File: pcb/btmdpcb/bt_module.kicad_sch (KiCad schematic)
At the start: 21 parts, among them J2 ANT, T1 ED8_4, T2 ED8_4

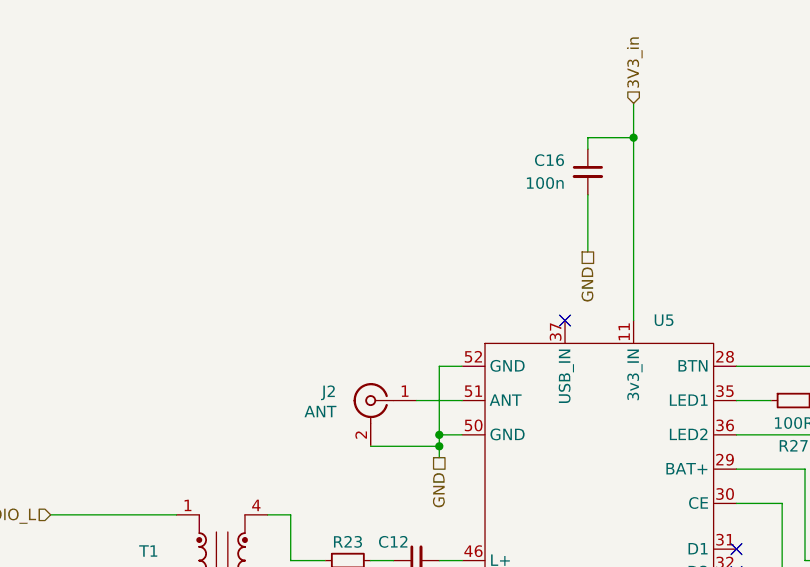
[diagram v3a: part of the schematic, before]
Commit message: Correct footprints, fix issues on update PCB from schematic
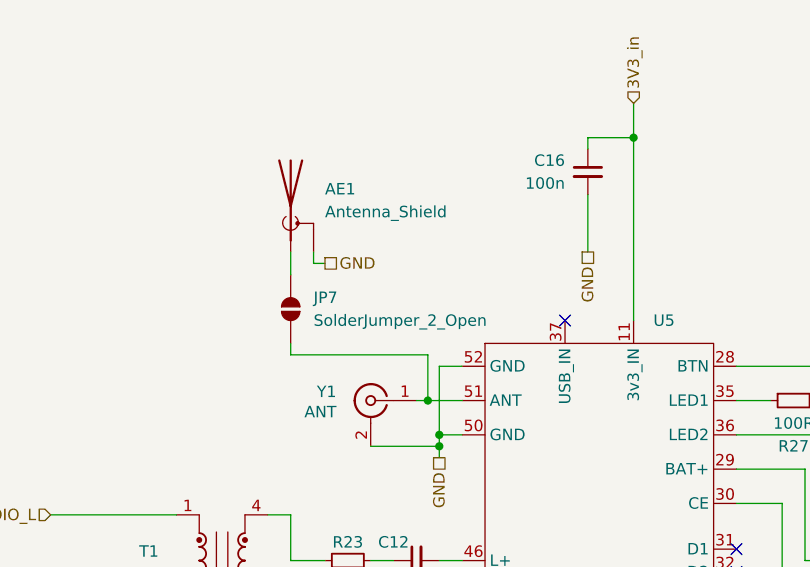
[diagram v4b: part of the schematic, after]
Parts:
- added AE1: Antenna_Shield, RF_Antenna:Texas_SWRA117D_2.4GHz_Right, symbol Device:Antenna_Shield
- added JP7: SolderJumper_2_Open, Jumper:SolderJumper-2_P1.3mm_Open_RoundedPad1.0x1.5mm, symbol Jumper:SolderJumper_2_Open
- renumbered J2 to Y1
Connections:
- net GND: now also AE1.2 (Shield)
- net at U5.51 (ANT), Y1.1 (In): now also JP7.2 (B)
- new net: AE1.1 (A), JP7.1 (A)
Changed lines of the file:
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@@
+	)
+	(junction
+		(at 120.65 83.82)
+		(diameter 0)
+		(color 0 0 0 0)
 	)
 	(junction
@@
 	(wire
 		(pts
-			(xy 119.38 83.82) (xy 124.46 83.82)
+			(xy 119.38 83.82) (xy 120.65 83.82)
 		)
 		(stroke
@@
 	(wire
 		(pts
+			(xy 120.65 83.82) (xy 124.46 83.82)
+		)
+		(stroke
+			(width 0)
+			(type default)
+		)
+	)
+	(wire
+		(pts
 			(xy 135.89 125.73) (xy 139.7 125.73)
 		)
@@
 	(wire
 		(pts
+			(xy 107.95 67.31) (xy 107.95 68.58)
+		)
+		(stroke
+			(width 0)
+			(type default)
+		)
+	)
+	(wire
+		(pts
 			(xy 121.92 90.17) (xy 121.92 88.9)
 		)
@@
 	(wire
 		(pts
+			(xy 105.41 67.31) (xy 105.41 69.85)
+		)
+		(stroke
+			(width 0)
+			(type default)
+		)
+	)
+	(wire
+		(pts
 			(xy 196.85 64.77) (xy 196.85 59.69)
 		)
@@
 	(wire
 		(pts
+			(xy 107.95 68.58) (xy 109.22 68.58)
+		)
+		(stroke
+			(width 0)
+			(type default)
+		)
+	)
+	(wire
+		(pts
 			(xy 139.7 123.19) (xy 139.7 125.73)
 		)
@@
 	(wire
 		(pts
+			(xy 105.41 78.74) (xy 120.65 78.74)
+		)
+		(stroke
+			(width 0)
+			(type default)
+		)
+	)
+	(wire
+		(pts
 			(xy 203.2 54.61) (xy 203.2 59.69)
 		)
@@
 	(wire
 		(pts
+			(xy 105.41 77.47) (xy 105.41 78.74)
+		)
+		(stroke
+			(width 0)
+			(type default)
+		)
+	)
+	(wire
+		(pts
 			(xy 121.92 88.9) (xy 121.92 87.63)
 		)
@@
 		(pts
 			(xy 154.94 91.44) (xy 162.56 91.44)
+		)
+		(stroke
+			(width 0)
+			(type default)
+		)
+	)
+	(wire
+		(pts
+			(xy 120.65 78.74) (xy 120.65 83.82)
 		)
 		(stroke
@@
 			)
 			(justify right)
+		)
+	)
+	(hierarchical_label "GND"
+		(shape passive)
+		(at 109.22 68.58 0)
+		(fields_autoplaced yes)
+		(effects
+			(font
+				(size 1.27 1.27)
+			)
+			(justify left)
 		)
 	)
@@
 	)
 	(symbol
+		(lib_id "Jumper:SolderJumper_2_Open")
+		(at 105.41 73.66 270)
+		(unit 1)
+		(exclude_from_sim yes)
+		(in_bom no)
+		(on_board yes)
+		(dnp no)
+		(fields_autoplaced yes)
+		(property "Reference" "JP7"
+			(at 107.95 72.3899 90)
+			(effects
+				(font
+					(size 1.27 1.27)
+				)
+				(justify left)
+			)
+		)
+		(property "Value" "SolderJumper_2_Open"
+			(at 107.95 74.9299 90)
+			(effects
+				(font
+					(size 1.27 1.27)
+				)
+				(justify left)
+			)
+		)
+		(property "Footprint" "Jumper:SolderJumper-2_P1.3mm_Open_RoundedPad1.0x1.5mm"
+			(at 105.41 73.66 0)
+			(effects
+				(font
+					(size 1.27 1.27)
+				)
+				(hide yes)
+			)
+		)
+		(property "Datasheet" "~"
+			(at 105.41 73.66 0)
+			(effects
+				(font
+					(size 1.27 1.27)
+				)
+				(hide yes)
+			)
+		)
+		(property "Description" "Solder Jumper, 2-pole, open"
+			(at 105.41 73.66 0)
+			(effects
+				(font
+					(size 1.27 1.27)
+				)
+				(hide yes)
+			)
+		)
+		(pin "2"
+		)
+		(pin "1"
+		)
+		(instances
+			(project ""
+				(path "/6e43e92f-e106-411c-86ee-217d084aee5b/5e29ed5f-7cd2-4605-9d5a-4da2465d4bbc"
+					(reference "JP7")
+					(unit 1)
+				)
+			)
+		)
+	)
+	(symbol
+		(lib_id "Device:Antenna_Shield")
+		(at 105.41 62.23 0)
+		(unit 1)
+		(exclude_from_sim no)
+		(in_bom yes)
+		(on_board yes)
+		(dnp no)
+		(fields_autoplaced yes)
+		(property "Reference" "AE1"
+			(at 109.22 60.3249 0)
+			(effects
+				(font
+					(size 1.27 1.27)
+				)
+				(justify left)
+			)
+		)
+		(property "Value" "Antenna_Shield"
+			(at 109.22 62.8649 0)
+			(effects
+				(font
+					(size 1.27 1.27)
+				)
+				(justify left)
+			)
+		)
+		(property "Footprint" "RF_Antenna:Texas_SWRA117D_2.4GHz_Right"
+			(at 105.41 59.69 0)
+			(effects
+				(font
+					(size 1.27 1.27)
+				)
+				(hide yes)
+			)
+		)
+		(property "Datasheet" "~"
+			(at 105.41 59.69 0)
+			(effects
+				(font
+					(size 1.27 1.27)
+				)
+				(hide yes)
+			)
+		)
+		(property "Description" "Antenna with extra pin for shielding"
+			(at 105.41 62.23 0)
+			(effects
+				(font
+					(size 1.27 1.27)
+				)
+				(hide yes)
+			)
+		)
+		(pin "1"
+		)
+		(pin "2"
+		)
+		(instances
+			(project ""
+				(path "/6e43e92f-e106-411c-86ee-217d084aee5b/5e29ed5f-7cd2-4605-9d5a-4da2465d4bbc"
+					(reference "AE1")
+					(unit 1)
+				)
+			)
+		)
+	)
+	(symbol
 		(lib_id "Device:C_Small")
 		(at 119.38 106.68 90)
@@
 		(on_board yes)
 		(dnp no)
-		(property "Reference" "J2"
+		(property "Reference" "Y1"
 			(at 110.49 82.8431 0)
 			(effects
@@
 			(project "btmdpcb"
 				(path "/6e43e92f-e106-411c-86ee-217d084aee5b/5e29ed5f-7cd2-4605-9d5a-4da2465d4bbc"
-					(reference "J2")
+					(reference "Y1")
 					(unit 1)
 				)

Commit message: Layout PCB
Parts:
- added C18: 100n, Capacitor_SMD:C_0805_2012Metric_Pad1.18x1.45mm_HandSolder, symbol Device:C_Small
- added C20: 100n, Capacitor_SMD:C_0805_2012Metric_Pad1.18x1.45mm_HandSolder, symbol Device:C
- added JP10: L_SKIP, Jumper:SolderJumper-2_P1.3mm_Open_RoundedPad1.0x1.5mm, symbol Jumper:SolderJumper_2_Bridged
- added JP12: USB_PWR, Jumper:SolderJumper-2_P1.3mm_Open_RoundedPad1.0x1.5mm, symbol Jumper:SolderJumper_2_Open
- added JP8: R_SKIP, Jumper:SolderJumper-2_P1.3mm_Open_RoundedPad1.0x1.5mm, symbol Jumper:SolderJumper_2_Bridged
- added JP9: AGND_SKIP, Jumper:SolderJumper-3_P1.3mm_Open_RoundedPad1.0x1.5mm, symbol Jumper:SolderJumper_3_Open
- added TP22: BT_L+, TestPoint:TestPoint_Pad_D1.0mm, symbol Connector:TestPoint
- added TP23: BT_L-, TestPoint:TestPoint_Pad_D1.0mm, symbol Connector:TestPoint
- added TP24: BT_R-, TestPoint:TestPoint_Pad_D1.0mm, symbol Connector:TestPoint
- added TP25: BT_R+, TestPoint:TestPoint_Pad_D1.0mm, symbol Connector:TestPoint
- added TP26: BT_USB_IN, TestPoint:TestPoint_Pad_D1.0mm, symbol Connector:TestPoint
- added TP27: BT_3V3, TestPoint:TestPoint_Pad_D1.0mm, symbol Connector:TestPoint
- added TP28: GND, TestPoint:TestPoint_Pad_D1.0mm, symbol Connector:TestPoint
- added TP29: BT_BTN, TestPoint:TestPoint_Pad_D1.0mm, symbol Connector:TestPoint
- AE1: footprint RF_Antenna:Texas_SWRA117D_2.4GHz_Right -> RF_Antenna:Texas_SWRA117D_2.4GHz_Left
- JP11: renamed from JP7; value SolderJumper_2_Open -> ANT
- TP30: renamed from TP8; value LED1 -> BT_LED1
- TP31: renamed from TP9; value LED2 -> BT_LED2
- TP32: renamed from TP6; value TestPoint -> BT_BAT+
- TP33: renamed from TP7; value TestPoint -> BT_CE
- renumbered C12 to C14, C13 to C15, C14 to C16, C15 to C17, C16 to C19, R23 to R25, R24 to R26, R25 to R27, R26 to R28, R27 to R29, R28 to R30, T2 to T1, T1 to T2
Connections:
- net 3V3_in: now also JP12.1 (A), TP27.1
- net AUDIO_GND: now also T1.3, JP9.2 (C); no longer T1.2
- net AUDIO_L: now also JP10.1 (A)
- net AUDIO_R: now also T1.4, JP8.1 (A); no longer T1.1
- net BTN: now also C20.2, TP29.1
- net GND: now also C18.2, C20.1, TP28.1
- net at R25.1, T2.4: now also JP10.2 (B)
- net at R27.1: now also T1.2, JP9.3 (B); no longer T1.3
- net at R28.1: now also T1.1, JP8.2 (B); no longer T1.4
- net at R29.1, U5.35 (LED1): now also TP30.1
- net at LED3.1 (K), R29.2: no longer TP30.1
- net at C15.2, U5.45 (L-): now also TP23.1
- net at R30.1: now also LED4.1 (K); no longer U5.36 (LED2)
- net at R30.2, TP31.1: now also U5.36 (LED2); no longer LED4.1 (K)
- net at R26.1, T2.3: now also JP9.1 (A)
- net at C16.2, U5.44 (R-): now also TP24.1
- net at C14.2, U5.46 (L+): now also TP22.1
- net at C17.2, U5.43 (R+): now also TP25.1
- net at U5.37 (USB_IN): now also C18.1, JP12.2 (B), TP26.1
- no-connect marks 9 -> 8
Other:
- moved on the sheet: AE1, C14, C15, C16, C17, C19, R25, R26, R27, R28, R29, R30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
